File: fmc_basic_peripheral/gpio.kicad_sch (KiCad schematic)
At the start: 43 parts, among them J6 PM2.54-2x6, SW1 DSHP04TSGET, SW10 TL3342F160QG, SW2 TL3342F160QG, SW8 TL3342F160QG, SW9 TL3342F160QG, U14 TXS02612RTWR

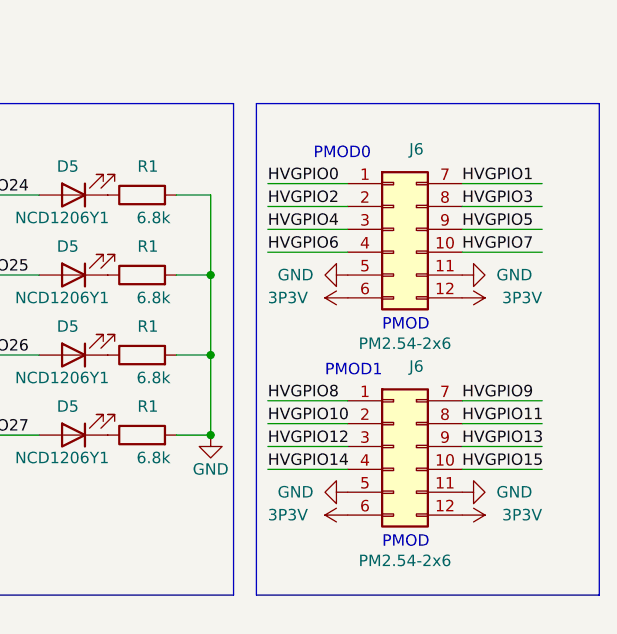
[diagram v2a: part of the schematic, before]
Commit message: fmc_basic_peripheral/gpio: fix net label and footprint
- Swap net label to match the latest footprint and PCB

Signed-off-by: Huang Rui <vowstar@gmail.com>
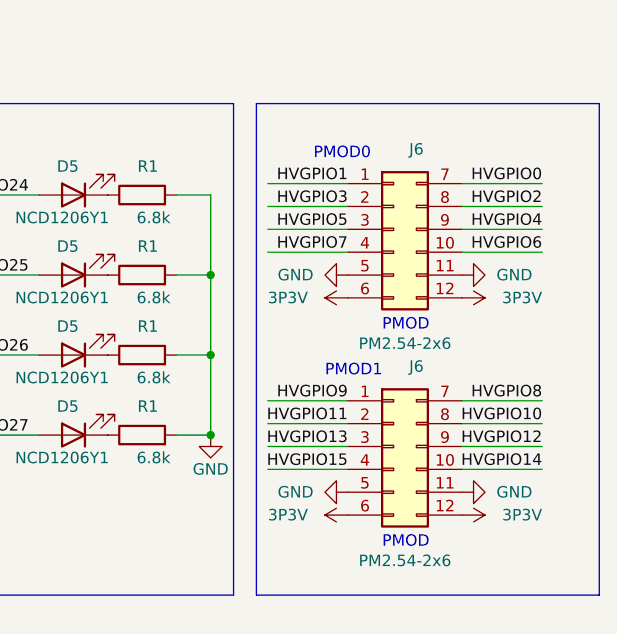
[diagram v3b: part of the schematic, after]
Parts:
- J6: footprint Connector_PinSocket_2.54mm:PinSocket_2x06_P2.54mm_Vertical -> CHIPSAlliance_Connector:PinSocket_2x06_P2.54mm_Vertical_PMOD
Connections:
- net HVGPIO0: now also J6.7 (Pin_7); no longer J6.1 (Pin_1)
- net HVGPIO1: now also J6.1 (Pin_1); no longer J6.7 (Pin_7)
- net HVGPIO10: now also J6.8 (Pin_8); no longer J6.2 (Pin_2)
- net HVGPIO11: now also J6.2 (Pin_2); no longer J6.8 (Pin_8)
- net HVGPIO12: now also J6.9 (Pin_9); no longer J6.3 (Pin_3)
- net HVGPIO13: now also J6.3 (Pin_3); no longer J6.9 (Pin_9)
- net HVGPIO14: now also J6.10 (Pin_10); no longer J6.4 (Pin_4)
- net HVGPIO15: now also J6.4 (Pin_4); no longer J6.10 (Pin_10)
- net HVGPIO2: now also J6.8 (Pin_8); no longer J6.2 (Pin_2)
- net HVGPIO3: now also J6.2 (Pin_2); no longer J6.8 (Pin_8)
- net HVGPIO4: now also J6.9 (Pin_9); no longer J6.3 (Pin_3)
- net HVGPIO5: now also J6.3 (Pin_3); no longer J6.9 (Pin_9)
- net HVGPIO6: now also J6.10 (Pin_10); no longer J6.4 (Pin_4)
- net HVGPIO7: now also J6.4 (Pin_4); no longer J6.10 (Pin_10)
- net HVGPIO8: now also J6.7 (Pin_7); no longer J6.1 (Pin_1)
- net HVGPIO9: now also J6.1 (Pin_1); no longer J6.7 (Pin_7)
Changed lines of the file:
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@@
     (title "GPIO")
     (date "2023-05-09")
-    (rev "1.0.6")
+    (rev "1.0.7")
     (company "CHIPS Alliance")
     (comment 1 "Rui Huang (2023-03-02)")
@@
     (effects (font (size 1.27 1.27)) (justify right bottom))
   )
-  (label "HVGPIO0" (at 243.84 50.8 0) (fields_autoplaced)
-    (effects (font (size 1.27 1.27)) (justify left bottom))
-  )
   (label "HVGPIO0" (at 69.85 50.8 180) (fields_autoplaced)
     (effects (font (size 1.27 1.27)) (justify right bottom))
@@
     (effects (font (size 1.27 1.27)) (justify left bottom))
   )
+  (label "HVGPIO15" (at 252.73 82.55 180) (fields_autoplaced)
+    (effects (font (size 1.27 1.27)) (justify right bottom))
+  )
   (label "HVGPIO17" (at 133.35 119.38 180) (fields_autoplaced)
     (effects (font (size 1.27 1.27)) (justify right bottom))
@@
     (effects (font (size 1.27 1.27)) (justify left bottom))
   )
+  (label "HVGPIO6" (at 274.32 58.42 180) (fields_autoplaced)
+    (effects (font (size 1.27 1.27)) (justify right bottom))
+  )
   (label "GPIO26" (at 21.59 127 0) (fields_autoplaced)
     (effects (font (size 1.27 1.27)) (justify left bottom))
@@
     (effects (font (size 1.27 1.27)) (justify left bottom))
   )
-  (label "HVGPIO13" (at 265.43 80.01 0) (fields_autoplaced)
-    (effects (font (size 1.27 1.27)) (justify left bottom))
-  )
-  (label "HVGPIO11" (at 265.43 77.47 0) (fields_autoplaced)
-    (effects (font (size 1.27 1.27)) (justify left bottom))
+  (label "HVGPIO9" (at 252.73 74.93 180) (fields_autoplaced)
+    (effects (font (size 1.27 1.27)) (justify right bottom))
   )
   (label "HVGPIO19" (at 148.59 128.27 0) (fields_autoplaced)
@@
     (effects (font (size 1.27 1.27)) (justify right bottom))
   )
+  (label "HVGPIO10" (at 274.32 77.47 180) (fields_autoplaced)
+    (effects (font (size 1.27 1.27)) (justify right bottom))
+  )
   (label "HVGPIO31" (at 195.58 58.42 180) (fields_autoplaced)
     (effects (font (size 1.27 1.27)) (justify right bottom))
   )
-  (label "HVGPIO8" (at 243.84 74.93 0) (fields_autoplaced)
-    (effects (font (size 1.27 1.27)) (justify left bottom))
-  )
   (label "HVGPIO2" (at 69.85 55.88 180) (fields_autoplaced)
     (effects (font (size 1.27 1.27)) (justify right bottom))
   )
+  (label "HVGPIO5" (at 252.73 55.88 180) (fields_autoplaced)
+    (effects (font (size 1.27 1.27)) (justify right bottom))
+  )
+  (label "HVGPIO3" (at 252.73 53.34 180) (fields_autoplaced)
+    (effects (font (size 1.27 1.27)) (justify right bottom))
+  )
+  (label "HVGPIO2" (at 274.32 53.34 180) (fields_autoplaced)
+    (effects (font (size 1.27 1.27)) (justify right bottom))
+  )
   (label "HVGPIO11" (at 132.08 53.34 180) (fields_autoplaced)
     (effects (font (size 1.27 1.27)) (justify right bottom))
@@
     (effects (font (size 1.27 1.27)) (justify right bottom))
   )
-  (label "HVGPIO5" (at 265.43 55.88 0) (fields_autoplaced)
-    (effects (font (size 1.27 1.27)) (justify left bottom))
-  )
   (label "GPIO30" (at 147.32 55.88 0) (fields_autoplaced)
     (effects (font (size 1.27 1.27)) (justify left bottom))
@@
     (effects (font (size 1.27 1.27)) (justify left bottom))
   )
-  (label "HVGPIO12" (at 243.84 80.01 0) (fields_autoplaced)
-    (effects (font (size 1.27 1.27)) (justify left bottom))
-  )
   (label "GPIO6" (at 21.59 116.84 0) (fields_autoplaced)
     (effects (font (size 1.27 1.27)) (justify left bottom))
@@
     (effects (font (size 1.27 1.27)) (justify left bottom))
   )
-  (label "HVGPIO4" (at 243.84 55.88 0) (fields_autoplaced)
-    (effects (font (size 1.27 1.27)) (justify left bottom))
-  )
   (label "GPIO[0..31]" (at 140.97 55.88 90) (fields_autoplaced)
     (effects (font (size 1.27 1.27)) (justify left bottom))
@@
     (effects (font (size 1.27 1.27)) (justify left bottom))
   )
-  (label "HVGPIO14" (at 243.84 82.55 0) (fields_autoplaced)
-    (effects (font (size 1.27 1.27)) (justify left bottom))
-  )
-  (label "HVGPIO6" (at 243.84 58.42 0) (fields_autoplaced)
-    (effects (font (size 1.27 1.27)) (justify left bottom))
-  )
   (label "HVGPIO30" (at 195.58 55.88 180) (fields_autoplaced)
     (effects (font (size 1.27 1.27)) (justify right bottom))
@@
     (effects (font (size 1.27 1.27)) (justify left bottom))
   )
+  (label "HVGPIO7" (at 252.73 58.42 180) (fields_autoplaced)
+    (effects (font (size 1.27 1.27)) (justify right bottom))
+  )
   (label "HVGPIO18" (at 133.35 121.92 180) (fields_autoplaced)
     (effects (font (size 1.27 1.27)) (justify right bottom))
@@
     (effects (font (size 1.27 1.27)) (justify right bottom))
   )
-  (label "HVGPIO15" (at 265.43 82.55 0) (fields_autoplaced)
-    (effects (font (size 1.27 1.27)) (justify left bottom))
+  (label "HVGPIO14" (at 274.32 82.55 180) (fields_autoplaced)
+    (effects (font (size 1.27 1.27)) (justify right bottom))
   )
   (label "GPIO14" (at 83.82 60.96 0) (fields_autoplaced)
     (effects (font (size 1.27 1.27)) (justify left bottom))
   )
-  (label "HVGPIO10" (at 243.84 77.47 0) (fields_autoplaced)
-    (effects (font (size 1.27 1.27)) (justify left bottom))
-  )
   (label "GPIO8" (at 21.59 121.92 0) (fields_autoplaced)
     (effects (font (size 1.27 1.27)) (justify left bottom))
   )
+  (label "HVGPIO1" (at 252.73 50.8 180) (fields_autoplaced)
+    (effects (font (size 1.27 1.27)) (justify right bottom))
+  )
   (label "HVGPIO7" (at 69.85 119.38 180) (fields_autoplaced)
     (effects (font (size 1.27 1.27)) (justify right bottom))
   )
+  (label "HVGPIO13" (at 252.73 80.01 180) (fields_autoplaced)
+    (effects (font (size 1.27 1.27)) (justify right bottom))
+  )
   (label "GPIO29" (at 147.32 53.34 0) (fields_autoplaced)
     (effects (font (size 1.27 1.27)) (justify left bottom))
   )
-  (label "HVGPIO2" (at 243.84 53.34 0) (fields_autoplaced)
-    (effects (font (size 1.27 1.27)) (justify left bottom))
+  (label "HVGPIO0" (at 274.32 50.8 180) (fields_autoplaced)
+    (effects (font (size 1.27 1.27)) (justify right bottom))
   )
   (label "GPIO1" (at 21.59 53.34 0) (fields_autoplaced)
     (effects (font (size 1.27 1.27)) (justify left bottom))
   )
+  (label "HVGPIO11" (at 252.73 77.47 180) (fields_autoplaced)
+    (effects (font (size 1.27 1.27)) (justify right bottom))
+  )
   (label "HVGPIO31" (at 215.9 128.27 0) (fields_autoplaced)
     (effects (font (size 1.27 1.27)) (justify left bottom))
@@
     (effects (font (size 1.27 1.27)) (justify right bottom))
   )
-  (label "HVGPIO1" (at 265.43 50.8 0) (fields_autoplaced)
-    (effects (font (size 1.27 1.27)) (justify left bottom))
-  )
-  (label "HVGPIO9" (at 265.43 74.93 0) (fields_autoplaced)
-    (effects (font (size 1.27 1.27)) (justify left bottom))
+  (label "HVGPIO12" (at 274.32 80.01 180) (fields_autoplaced)
+    (effects (font (size 1.27 1.27)) (justify right bottom))
   )
   (label "HVGPIO27" (at 208.28 78.74 0) (fields_autoplaced)
     (effects (font (size 1.27 1.27)) (justify left bottom))
   )
-  (label "HVGPIO7" (at 265.43 58.42 0) (fields_autoplaced)
-    (effects (font (size 1.27 1.27)) (justify left bottom))
-  )
   (label "GPIO27" (at 85.09 127 0) (fields_autoplaced)
     (effects (font (size 1.27 1.27)) (justify left bottom))
@@
     (effects (font (size 1.27 1.27)) (justify left bottom))
   )
-  (label "HVGPIO3" (at 265.43 53.34 0) (fields_autoplaced)
-    (effects (font (size 1.27 1.27)) (justify left bottom))
+  (label "HVGPIO4" (at 274.32 55.88 180) (fields_autoplaced)
+    (effects (font (size 1.27 1.27)) (justify right bottom))
   )
   (label "HVGPIO29" (at 195.58 53.34 180) (fields_autoplaced)
@@
   (label "HVGPIO26" (at 208.28 69.85 0) (fields_autoplaced)
     (effects (font (size 1.27 1.27)) (justify left bottom))
+  )
+  (label "HVGPIO8" (at 274.32 74.93 180) (fields_autoplaced)
+    (effects (font (size 1.27 1.27)) (justify right bottom))
   )
   (label "HVGPIO16" (at 133.35 116.84 180) (fields_autoplaced)
@@
       (effects (font (size 1.27 1.27)))
     )
-    (property "Footprint" "Connector_PinSocket_2.54mm:PinSocket_2x06_P2.54mm_Vertical" (at 256.54 49.53 0)
+    (property "Footprint" "CHIPSAlliance_Connector:PinSocket_2x06_P2.54mm_Vertical_PMOD" (at 256.54 49.53 0)
       (effects (font (size 1.27 1.27)) hide)
     )
@@
       (effects (font (size 1.27 1.27)))
     )
-    (property "Footprint" "Connector_PinSocket_2.54mm:PinSocket_2x06_P2.54mm_Vertical" (at 256.54 73.66 0)
-      (effects (font (size 1.27 1.27)) hide)
-    )
+    (property "Footprint" "CHIPSAlliance_Connector:PinSocket_2x06_P2.54mm_Vertical_PMOD" (at 256.54 73.66 0)
+      (effects (font (size 1.27 1.27)) hide)
+    )

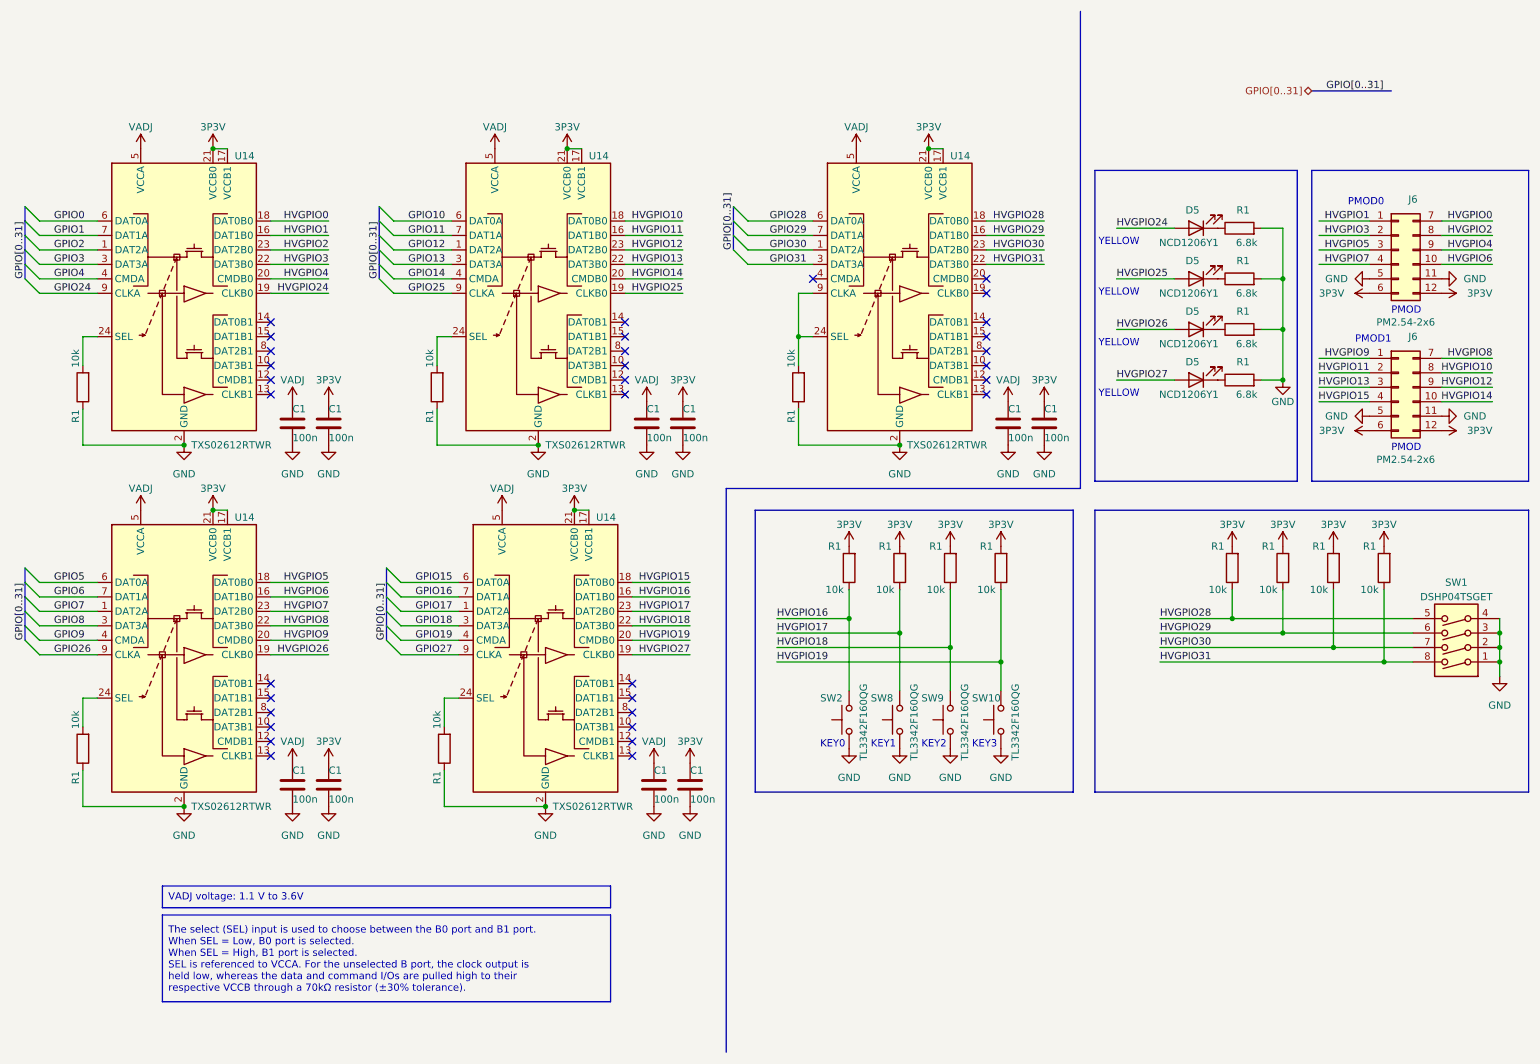
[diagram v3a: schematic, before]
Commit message: fmc_basic_peripheral: Migrate to kicad8
- Migrate schematics to kicad8
- Migrate PCB to kicad8
- Clean ERC
- Clean LVS and DRC

Signed-off-by: Huang Rui <vowstar@gmail.com>
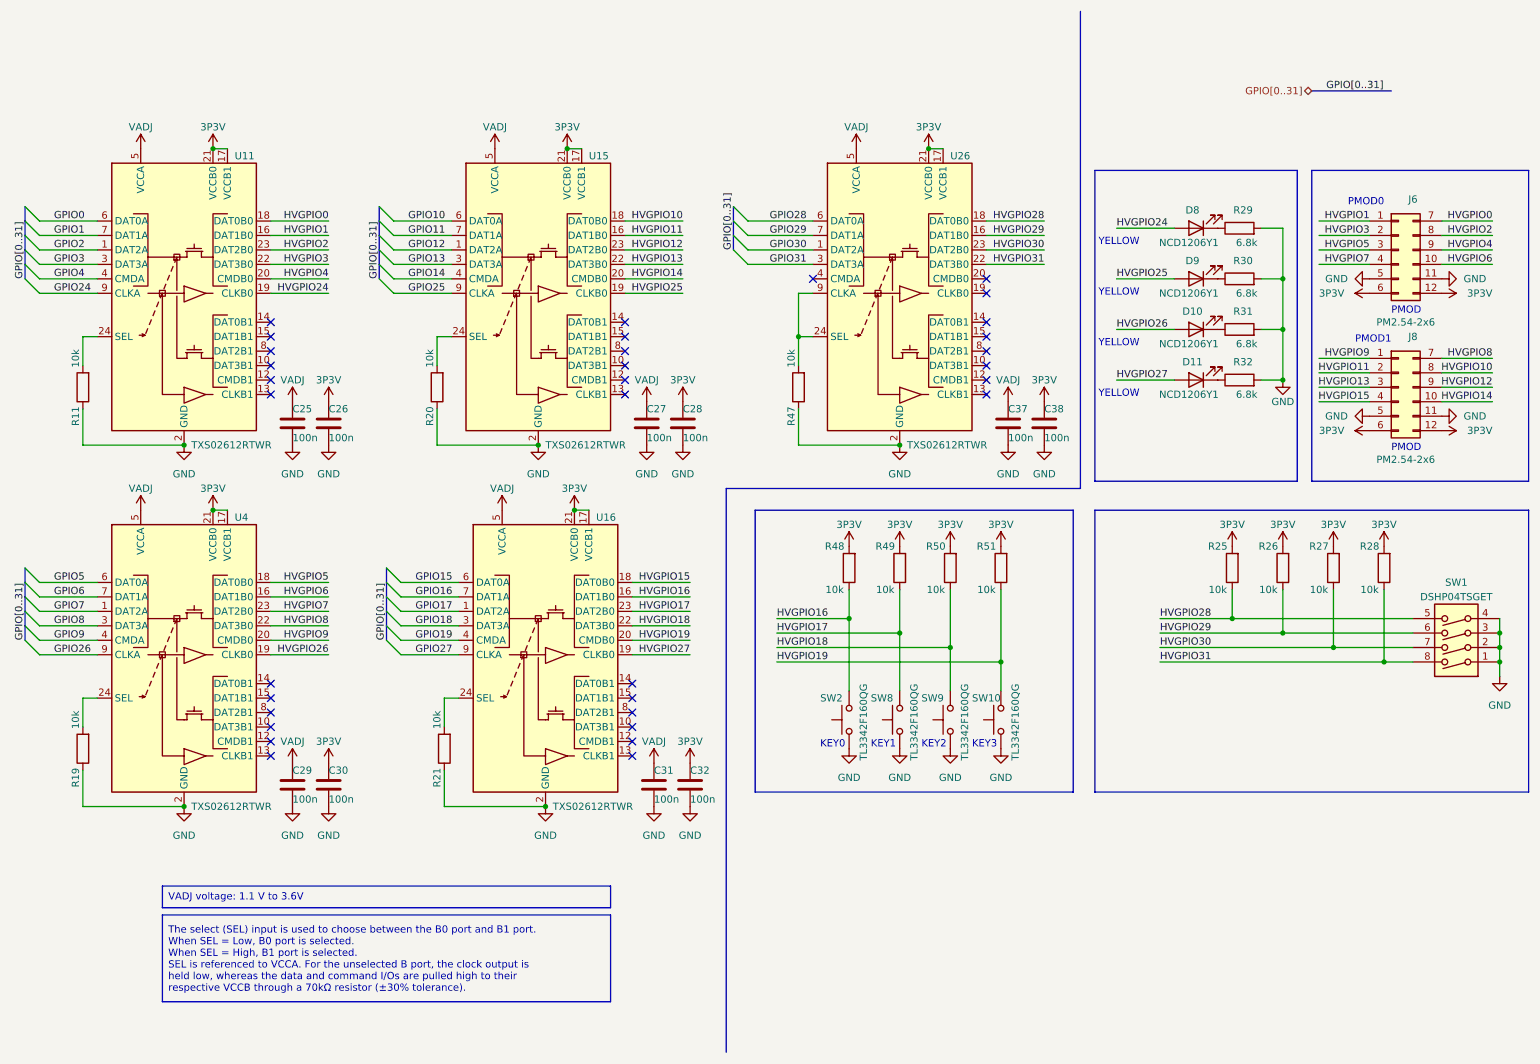
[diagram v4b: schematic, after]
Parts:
- renumbered C1 to C25, C1 to C26, C1 to C27, C1 to C28, C1 to C29, C1 to C30, C1 to C31, C1 to C32, C1 to C37, C1 to C38, D5 to D10, D5 to D11, D5 to D8, D5 to D9, J6 to J8, R1 to R11, R1 to R19, R1 to R20, R1 to R21, R1 to R25, R1 to R26, R1 to R27, R1 to R28, R1 to R29, R1 to R30, R1 to R31, R1 to R32, R1 to R47, R1 to R48, R1 to R49, R1 to R50, R1 to R51, U14 to U11, U14 to U15, U14 to U16, U14 to U26, U14 to U4
